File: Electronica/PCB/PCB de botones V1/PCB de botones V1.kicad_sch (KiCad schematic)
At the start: 14 parts, among them J1 Conn_02x05_Counter_Clockwise, SW1 SW_Push, SW2 SW_Push, SW3 SW_SPST

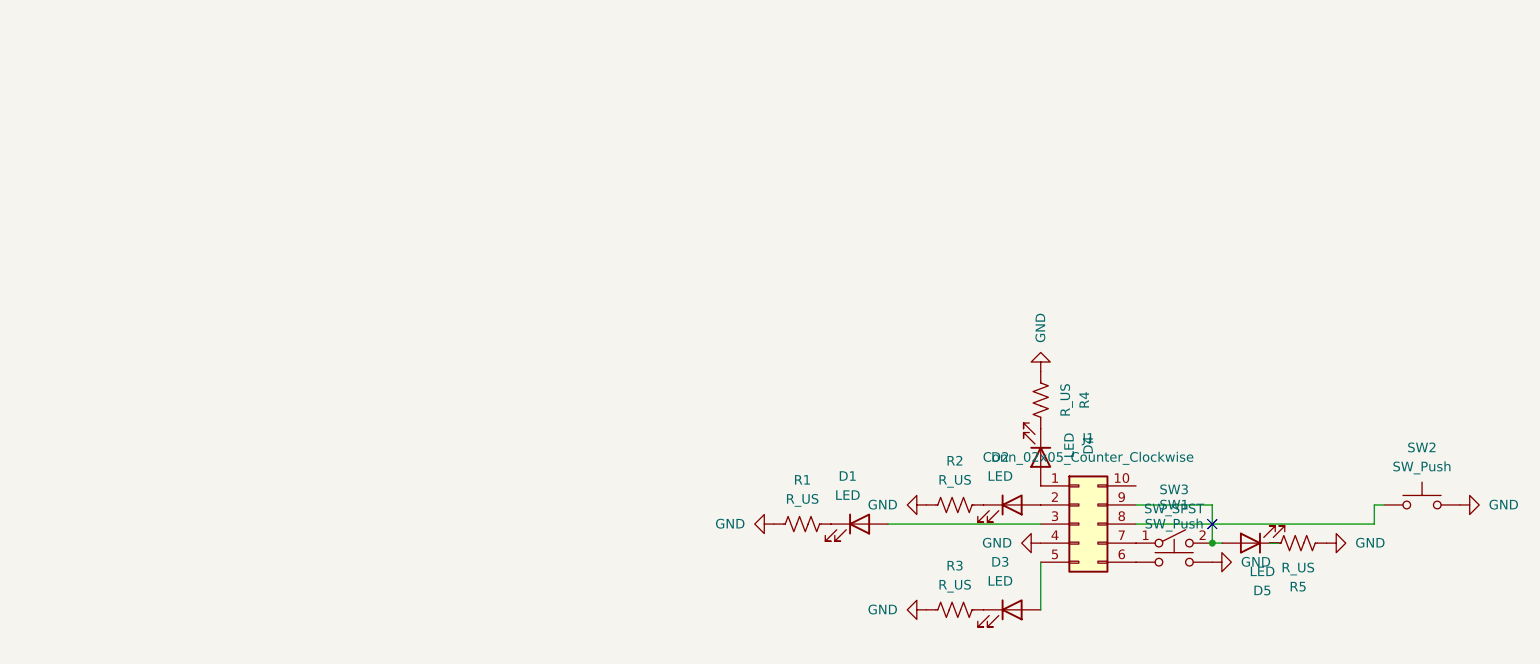
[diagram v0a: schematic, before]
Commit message: PCB de botones terminada
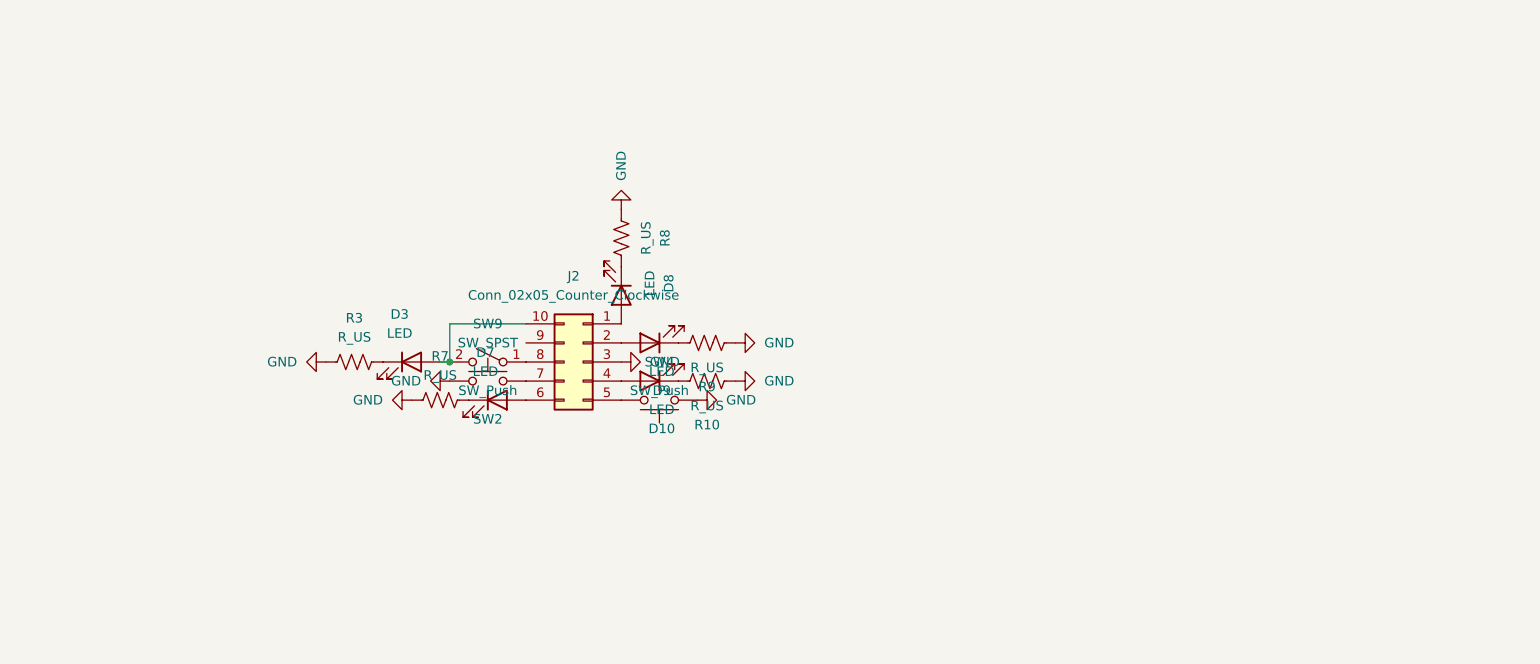
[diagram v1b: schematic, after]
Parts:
- removed D1, D2, D4, D5: LED, LED_THT:LED_D5.0mm, symbol Device:LED
- removed J1: Conn_02x05_Counter_Clockwise, Connector_IDC:IDC-Header_2x05_P2.54mm_Vertical, symbol Connector_Generic:Conn_02x05_Counter_Clockwise
- removed R1, R2, R4, R5: R_US, Resistor_THT:R_Axial_DIN0207_L6.3mm_D2.5mm_P10.16mm_Horizontal, symbol Device:R_US
- removed SW1: SW_Push, Button_Switch_THT:SW_PUSH_6mm, symbol Switch:SW_Push
- removed SW3: SW_SPST, Button_Switch_THT:SW_Slide_SPDT_Straight_CK_OS102011MS2Q, symbol Switch:SW_SPST
- added D10, D7, D8, D9: LED, LED_THT:LED_D5.0mm, symbol Device:LED
- added J2: Conn_02x05_Counter_Clockwise, Connector_IDC:IDC-Header_2x05_P2.54mm_Vertical, symbol Connector_Generic:Conn_02x05_Counter_Clockwise
- added R10, R7, R8, R9: R_US, Resistor_THT:R_Axial_DIN0207_L6.3mm_D2.5mm_P10.16mm_Horizontal, symbol Device:R_US
- added SW4: SW_Push, Button_Switch_THT:SW_PUSH_6mm, symbol Switch:SW_Push
- added SW9: SW_SPST, Button_Switch_THT:SW_Slide_SPDT_Straight_CK_OS102011MS2Q, symbol Switch:SW_SPST
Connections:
- net GND: now also J2.3 (Pin_3), R10.1, R7.1, R8.1, R9.1, SW4.2
- net at SW2.1: now also J2.7 (Pin_7)
- net at D3.2 (A): now also J2.10 (Pin_10), SW9.2 (B)
- new net: D9.1 (K), R9.2
- new net: D9.2 (A), J2.2 (Pin_2)
- new net: J2.5 (Pin_5), SW4.1
- new net: D8.2 (A), J2.1 (Pin_1)
- new net: D10.2 (A), J2.4 (Pin_4)
- new net: D7.2 (A), J2.6 (Pin_6)
- new net: J2.8 (Pin_8), SW9.1 (A)
- new net: D10.1 (K), R10.2
- new net: D7.1 (K), R7.2
- new net: D8.1 (K), R8.2
- no-connect marks 1 -> 0

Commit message: .
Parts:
- added J1: IDC Placa Botones, Connector_IDC:IDC-Header_2x05_P2.54mm_Horizontal, symbol Connector_Generic:Conn_02x05_Counter_Clockwise
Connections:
- net GND: now also J1.1 (Pin_1)
- new net BTN1: J1.5 (Pin_5)
- new net BTN2: J1.3 (Pin_3)
- new net LED1: J1.7 (Pin_7)
- new net LED2: J1.2 (Pin_2)
- new net LED3: J1.4 (Pin_4)
- new net LED4: J1.6 (Pin_6)
- no-connect marks 0 -> 3
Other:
- note added: "Hola cherniak como estas tanto tiempo Te dejo las conexiones corregidas al IDC Por favor esta vez hace un esquematico un poquito mas lindo..."

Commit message: pcb de leds
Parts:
- removed D10, D7, D8, D9: LED, LED_THT:LED_D5.0mm, symbol Device:LED
- removed J2: Conn_02x05_Counter_Clockwise, Connector_IDC:IDC-Header_2x05_P2.54mm_Vertical, symbol Connector_Generic:Conn_02x05_Counter_Clockwise
- removed R10, R7, R8, R9: R_US, Resistor_THT:R_Axial_DIN0207_L6.3mm_D2.5mm_P10.16mm_Horizontal, symbol Device:R_US
- removed SW4: SW_Push, Button_Switch_THT:SW_PUSH_6mm, symbol Switch:SW_Push
- removed SW9: SW_SPST, Button_Switch_THT:SW_Slide_SPDT_Straight_CK_OS102011MS2Q, symbol Switch:SW_SPST
- added D1, D2, D4: LED, LED_THT:LED_D5.0mm, symbol Device:LED
- added R1, R2, R4: R_US, Resistor_THT:R_Axial_DIN0207_L6.3mm_D2.5mm_P10.16mm_Horizontal, symbol Device:R_US
- added SW1: SW_Push, Button_Switch_THT:SW_PUSH_6mm, symbol Switch:SW_Push
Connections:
- net BTN1: now also SW1.1
- net BTN2: now also SW2.1
- net GND: now also R1.1, R2.1, R4.1, SW1.2
- net LED1: now also D1.2 (A)
- net LED2: now also D2.2 (A)
- net LED3: now also D3.2 (A)
- net LED4: now also D4.2 (A)
- new net: D2.1 (K), R2.2
- new net: D4.1 (K), R4.2
- new net: D1.1 (K), R1.2
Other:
- note added: "BOTONES"
- note added: "LEDS"
- note removed: "Hola cherniak como estas tanto tiempo Te dejo las conexiones corregidas al IDC Por favor esta vez hace un esquematico un poquito mas lindo..."
- moved on the sheet: J1
